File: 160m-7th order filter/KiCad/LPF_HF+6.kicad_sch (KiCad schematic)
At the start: 129 parts, among them J1 Conn_01x07, J2 12V INPUT, J3 LFP_IN, J4 Conn_01x07, J5 RF output, U1 AMS1117-5, U2 74AHC595, U3 ULN2003

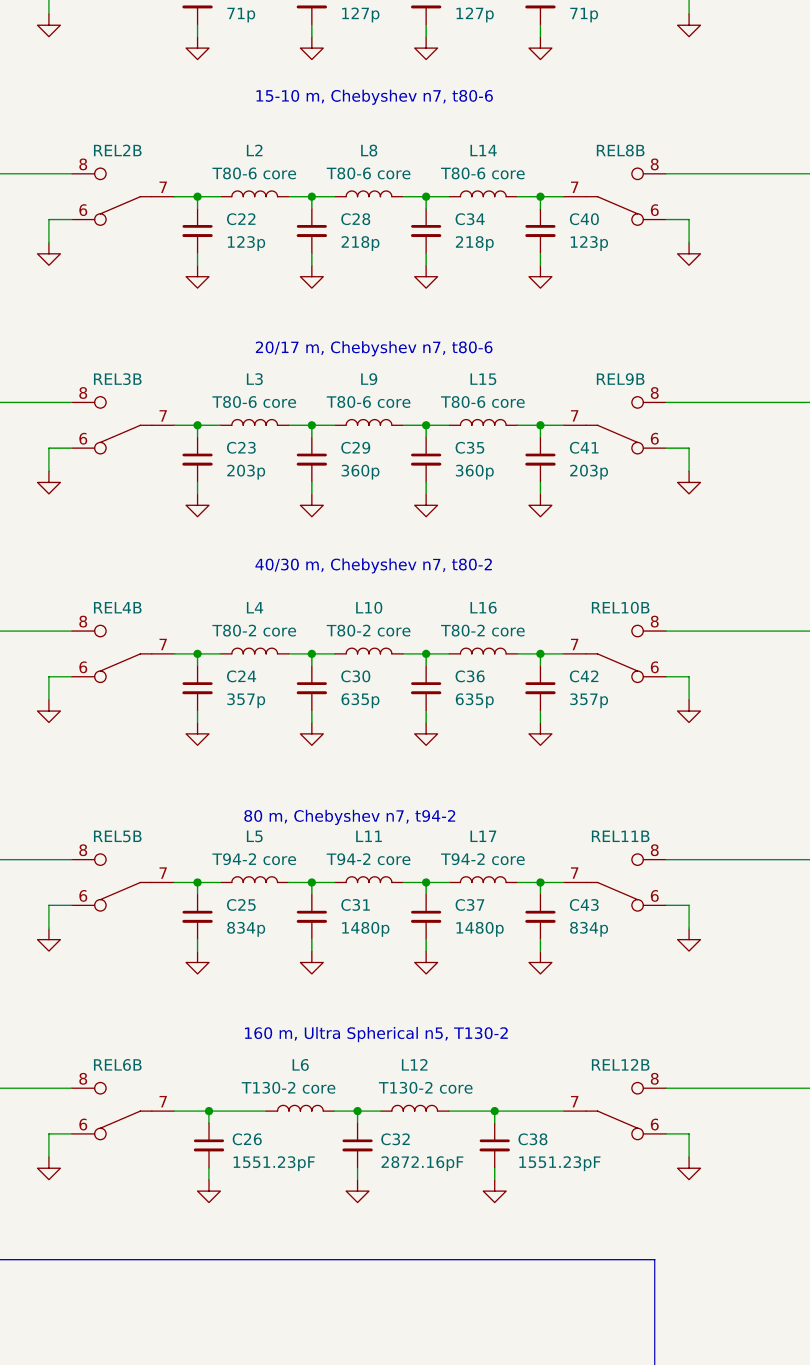
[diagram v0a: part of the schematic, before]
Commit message: 160m Cheby7
Created and Updated 160m 7th Order Filter Design
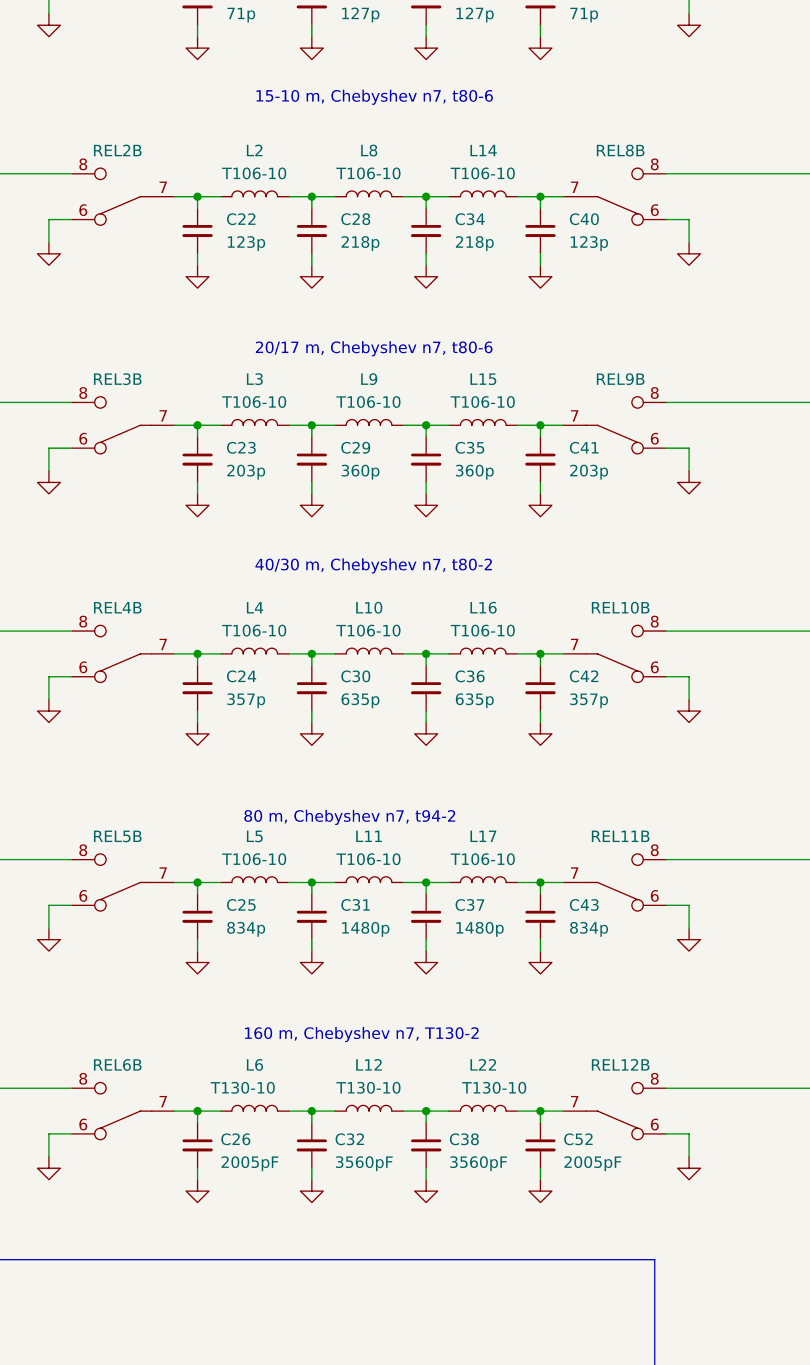
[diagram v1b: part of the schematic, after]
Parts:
- added C52: 2005pF, LPF_Footprints:4x1206_2, symbol Device:C_Small
- added L22: T130-10, LPF_Footprints:T106-Inductor, symbol Device:L
- C26: value 1551.23pF -> 2005pF; footprint LPF_Footprints:6x1206 -> LPF_Footprints:4x1206_2
- C32: value 2872.16pF -> 3560pF
- C38: value 1551.23pF -> 3560pF
- L10, L16, L4: value T80-2 core -> T106-10
- L11, L17, L5: value T94-2 core -> T106-10
- L12, L6: value T130-2 core -> T130-10
- L14, L15, L2, L3, L8, L9: value T80-6 core -> T106-10
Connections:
- net GND: now also C52.2
- net at C38.1, L12.2: now also L22.1; no longer REL12.4, REL12.7
- new net: C52.1, L22.2, REL12.4, REL12.7
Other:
- note added: "160 m, Chebyshev n7, T130-2"
- note removed: "160 m, Ultra Spherical n5, T130-2"
- moved on the sheet: C26, C32, C38, L12, L6

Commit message: General Save
Minor updates and improvements
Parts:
- C21, C22, C23, C24, C25, C26, C27, C28, C29, C30, C31, C33, C34, C35, C36, C37, C39, C40, C41, C42, C43, C52: MPN (none) -> Refer
- C32, C38: footprint LPF_Footprints:6x1206 -> LPF_Footprints:6x1206_3x2; MPN (none) -> Refer
- L1, L10, L11, L13, L14, L15, L16, L17, L2, L3, L4, L5, L7, L8, L9: footprint LPF_Footprints:T94-6_Inductor -> LPF_Footprints:T106-Inductor

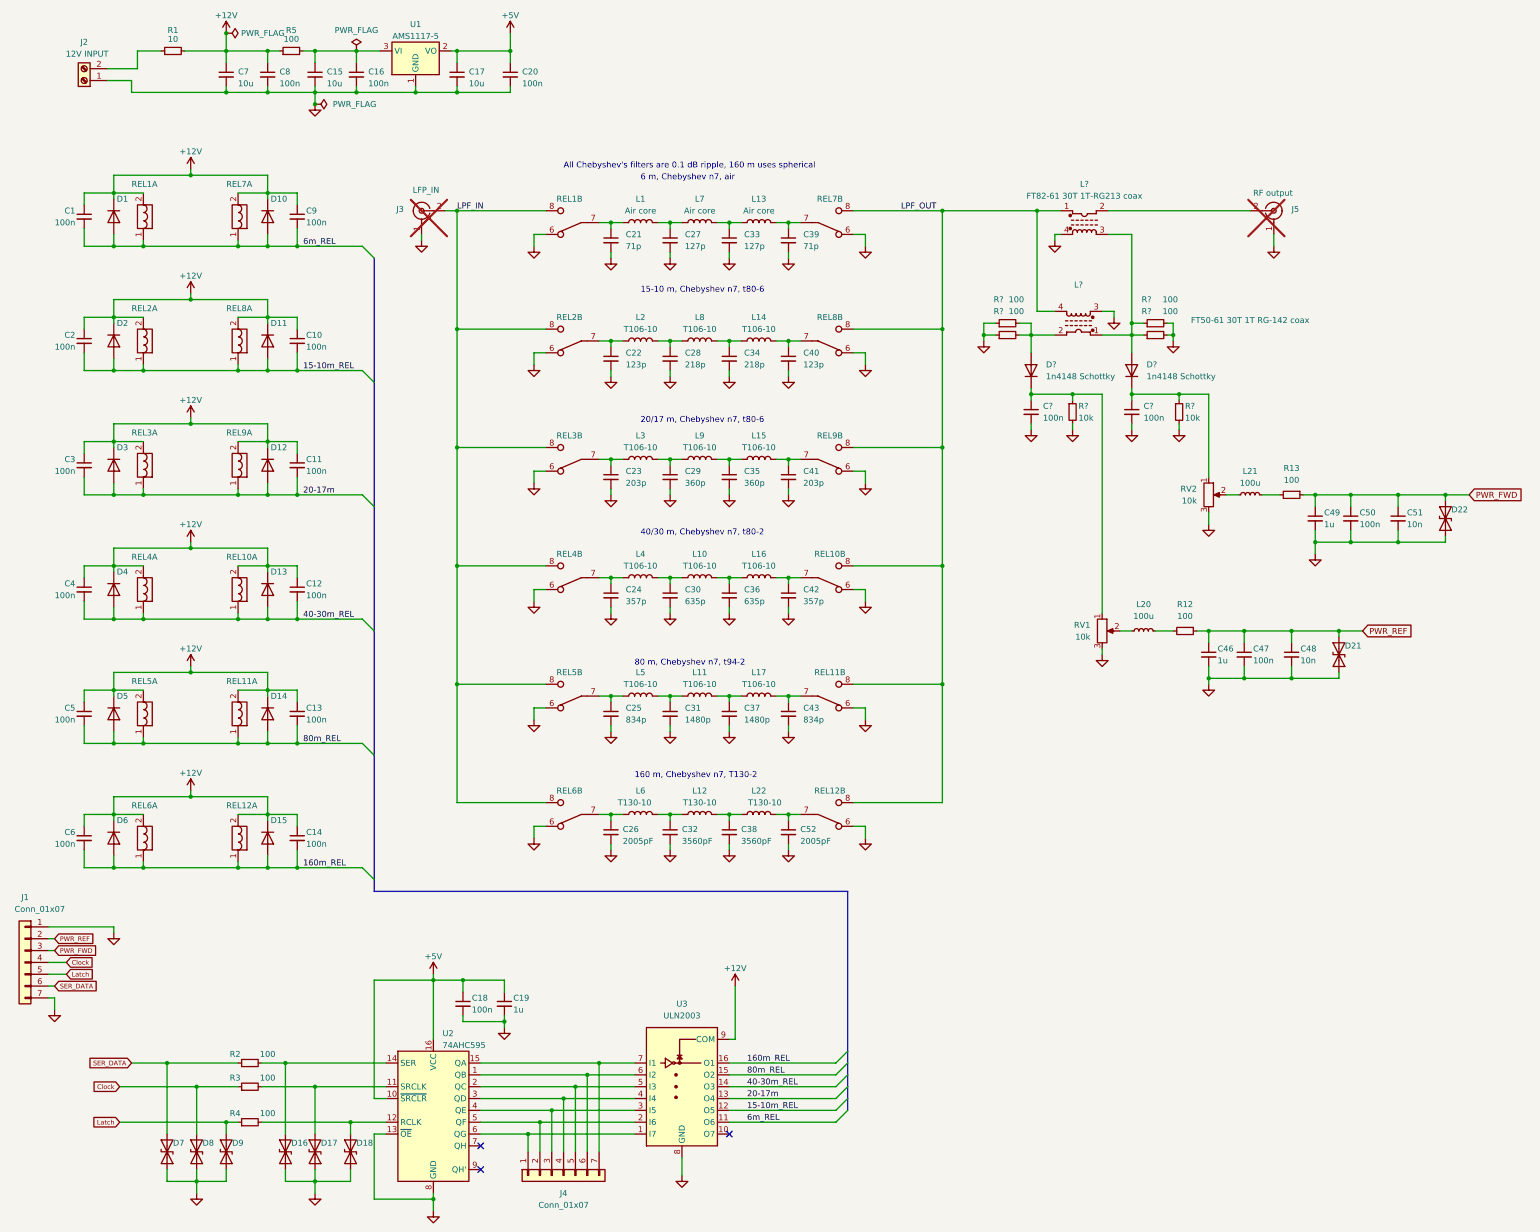
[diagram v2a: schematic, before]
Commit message: LPF capacitor and toroid selections improved
Added separate sheet for documenting capacitor makeup.
reflected in BOM much more accurately.
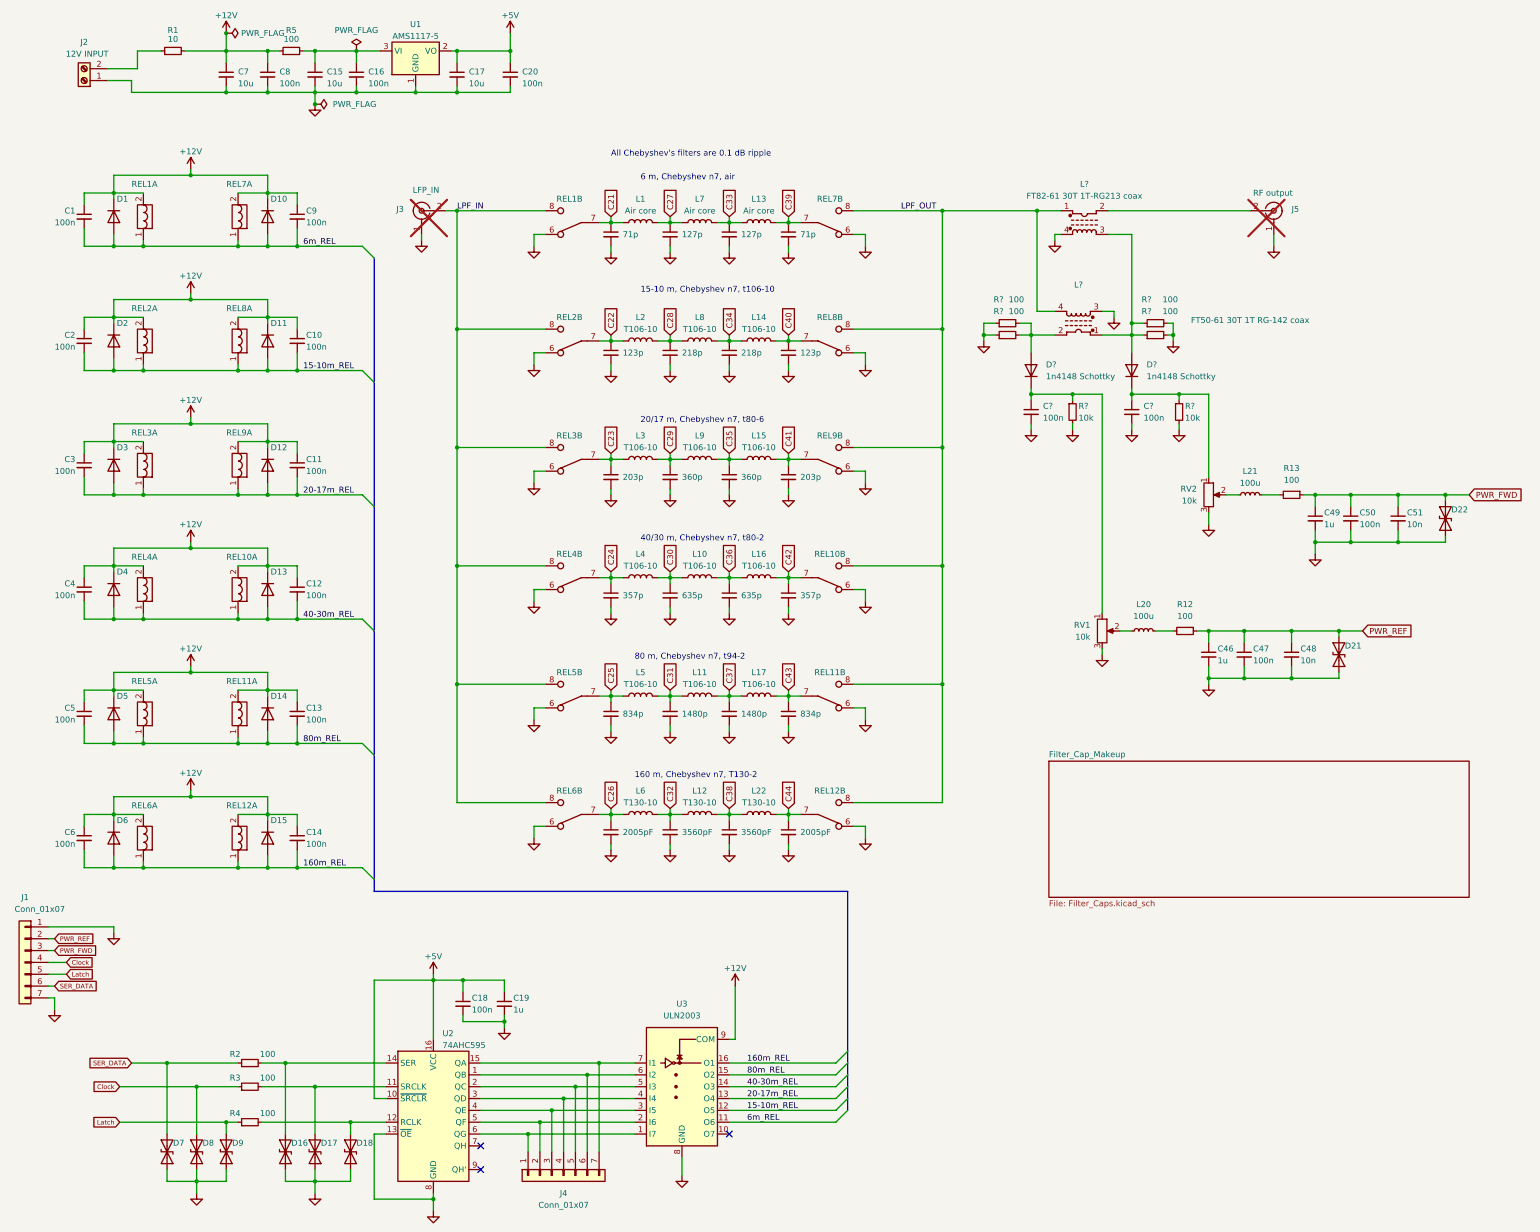
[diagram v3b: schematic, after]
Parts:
- C21, C22, C24, C25, C26, C27, C28, C29, C30, C31, C33, C34, C35, C36, C37, C39, C40, C41, C42, C43: footprint LPF_Footprints:4x1206_2 -> (none); now left out of the parts list
- C23: now left out of the parts list
- C32, C38: footprint LPF_Footprints:6x1206_3x2 -> (none); now left out of the parts list
- C44: renamed from C52; footprint LPF_Footprints:4x1206_2 -> (none); now left out of the parts list
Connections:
- net C32: now reaches C32.1, L12.1, L6.2
- net C25: now reaches C25.1, L5.1, REL5.4, REL5.7
- net C21: now reaches C21.1, L1.1, REL1.4, REL1.7
- net C27: now reaches C27.1, L1.2, L7.1
- net C22: now reaches C22.1, L2.1, REL2.4, REL2.7
- net C23: now reaches C23.1, L3.1, REL3.4, REL3.7
- net C24: now reaches C24.1, L4.1, REL4.4, REL4.7
- net C30: now reaches C30.1, L10.1, L4.2
- net C36: now reaches C36.1, L10.2, L16.1
- net C38: now reaches C38.1, L12.2, L22.1
- net C42: now reaches C42.1, L16.2, REL10.4, REL10.7
- net C44: now reaches C44.1, L22.2, REL12.4, REL12.7
- net C33: now reaches C33.1, L13.1, L7.2
- net C39: now reaches C39.1, L13.2, REL7.4, REL7.7
- net C31: now reaches C31.1, L11.1, L5.2
- net C40: now reaches C40.1, L14.2, REL8.4, REL8.7
- net C43: now reaches C43.1, L17.2, REL11.4, REL11.7
- net C35: now reaches C35.1, L15.1, L9.2
- net C41: now reaches C41.1, L15.2, REL9.4, REL9.7
- net C29: now reaches C29.1, L3.2, L9.1
- net C26: now reaches C26.1, L6.1, REL6.4, REL6.7
- net C34: now reaches C34.1, L14.1, L8.2
- net C37: now reaches C37.1, L11.2, L17.1
- net C28: now reaches C28.1, L2.2, L8.1
- net 20-17m renamed 20-17m_REL
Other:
- added sheet Filter_Cap_Makeup (Filter_Caps.kicad_sch)
- note added: "15-10 m, Chebyshev n7, t106-10"
- note added: "All Chebyshev's filters are 0.1 dB ripple"
- note removed: "15-10 m, Chebyshev n7, t80-6"
- note removed: "All Chebyshev's filters are 0.1 dB ripple, 160 m uses spherical"
